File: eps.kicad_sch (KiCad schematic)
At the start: 14 parts

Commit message: added
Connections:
- net GND: now reaches SC1.2 (-), SC2.2 (-), SC3.2 (-), SC4.2 (-), SC5.2 (-), SC6.2 (-)
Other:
- sheet BatteryCharger ports: added gnd; removed none
- sheet BatteryCharger1 ports: added gnd; removed none
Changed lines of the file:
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@@
   (junction (at 64.77 64.77) (diameter 0) (color 0 0 0 0)
   )
+  (junction (at 46.99 121.92) (diameter 0) (color 0 0 0 0)
+  )
   (junction (at 46.99 80.01) (diameter 0) (color 0 0 0 0)
   )
@@
     (stroke (width 0) (type default))
   )
+  (wire (pts (xy 100.33 67.31) (xy 95.25 67.31))
+    (stroke (width 0) (type default))
+  )
   (wire (pts (xy 125.73 107.95) (xy 130.81 107.95))
     (stroke (width 0) (type default))
@@
     (stroke (width 0) (type default))
   )
+  (wire (pts (xy 97.79 110.49) (xy 102.87 110.49))
+    (stroke (width 0) (type default))
+  )
   (wire (pts (xy 138.43 85.09) (xy 138.43 107.95))
     (stroke (width 0) (type default))
@@
     (stroke (width 0) (type default))
   )
+  (wire (pts (xy 95.25 67.31) (xy 95.25 72.39))
+    (stroke (width 0) (type default))
+  )
   (wire (pts (xy 46.99 80.01) (xy 46.99 93.98))
     (stroke (width 0) (type default))
@@
     (stroke (width 0) (type default))
   )
+  (wire (pts (xy 97.79 118.11) (xy 97.79 110.49))
+    (stroke (width 0) (type default))
+  )
   (symbol (lib_id "Device:Solar_Cells") (at 52.07 93.98 270) (unit 1)
     (in_bom yes) (on_board yes) (dnp no) (fields_autoplaced)
@@
     )
   )
+  (symbol (lib_id "power:GND") (at 46.99 121.92 0) (unit 1)
+    (in_bom yes) (on_board yes) (dnp no) (fields_autoplaced)
+    (property "Reference" "#PWR04" (at 46.99 128.27 0)
+      (effects (font (size 1.27 1.27)) hide)
+    )
+    (property "Value" "GND" (at 46.99 127 0)
+      (effects (font (size 1.27 1.27)))
+    )
+    (property "Footprint" "" (at 46.99 121.92 0)
+      (effects (font (size 1.27 1.27)) hide)
+    )
+    (property "Datasheet" "" (at 46.99 121.92 0)
+      (effects (font (size 1.27 1.27)) hide)
+    )
+    (pin "1")
+    (instances
+      (project "eps"
+        (path "/d1becec8-2a81-45a7-bfc6-f9ad93456edc"
+          (reference "#PWR04") (unit 1)
+        )
+      )
+    )
+  )
   (symbol (lib_id "Device:D_Schottky") (at 60.96 121.92 180) (unit 1)
     (in_bom yes) (on_board yes) (dnp no) (fields_autoplaced)
@@
     )
   )
+  (symbol (lib_id "power:GND") (at 97.79 118.11 0) (unit 1)
+    (in_bom yes) (on_board yes) (dnp no) (fields_autoplaced)
+    (property "Reference" "#PWR03" (at 97.79 124.46 0)
+      (effects (font (size 1.27 1.27)) hide)
+    )
+    (property "Value" "GND" (at 97.79 123.19 0)
+      (effects (font (size 1.27 1.27)))
+    )
+    (property "Footprint" "" (at 97.79 118.11 0)
+      (effects (font (size 1.27 1.27)) hide)
+    )
+    (property "Datasheet" "" (at 97.79 118.11 0)
+      (effects (font (size 1.27 1.27)) hide)
+    )
+    (pin "1")
+    (instances
+      (project "eps"
+        (path "/d1becec8-2a81-45a7-bfc6-f9ad93456edc"
+          (reference "#PWR03") (unit 1)
+        )
+      )
+    )
+  )
   (symbol (lib_id "Device:Solar_Cells") (at 52.07 64.77 270) (unit 1)
     (in_bom yes) (on_board yes) (dnp no) (fields_autoplaced)
@@
         (path "/d1becec8-2a81-45a7-bfc6-f9ad93456edc"
           (reference "SC1") (unit 1)
+        )
+      )
+    )
+  )
+  (symbol (lib_id "power:GND") (at 95.25 72.39 0) (unit 1)
+    (in_bom yes) (on_board yes) (dnp no) (fields_autoplaced)
+    (property "Reference" "#PWR02" (at 95.25 78.74 0)
+      (effects (font (size 1.27 1.27)) hide)
+    )
+    (property "Value" "GND" (at 95.25 77.47 0)
+      (effects (font (size 1.27 1.27)))
+    )
+    (property "Footprint" "" (at 95.25 72.39 0)
+      (effects (font (size 1.27 1.27)) hide)
+    )
+    (property "Datasheet" "" (at 95.25 72.39 0)
+      (effects (font (size 1.27 1.27)) hide)
+    )
+    (pin "1")
+    (instances
+      (project "eps"
+        (path "/d1becec8-2a81-45a7-bfc6-f9ad93456edc"
+          (reference "#PWR02") (unit 1)
         )
       )
@@
       (effects (font (size 1.27 1.27)) (justify right))
     )
+    (pin "gnd" input (at 102.87 110.49 180)
+      (effects (font (size 1.27 1.27)) (justify left))
+    )
     (instances
       (project "eps"
@@
       (effects (font (size 1.27 1.27)) (justify right))
     )
-    (instances
+    (pin "gnd" input (at 100.33 67.31 180)
+      (effects (font (size 1.27 1.27)) (justify left))
+    )
+    (instances

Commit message: v0.1Hydrogen
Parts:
- removed D7, D8: D_Schottky, symbol Device:D_Schottky
- D1, D2, D3, D4, D5, D6: footprint (none) -> Diode_THT:D_DO-35_SOD27_P7.62mm_Horizontal
- SC1, SC2, SC3, SC4, SC5, SC6: footprint (none) -> Connector_PinHeader_1.00mm:PinHeader_2x01_P1.00mm_Vertical
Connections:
- net BatteryCharger1/in is gone; now on net BatteryCharger/in: D4.1 (K), D5.1 (K), D6.1 (K)
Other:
- removed sheet BatteryCharger1
- sheet BatteryCharger ports: added none; removed gnd

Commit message: Solved errors
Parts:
- added J2: Conn_01x02_Pin, Connector_PinHeader_2.00mm:PinHeader_1x02_P2.00mm_Vertical, symbol Connector:Conn_01x02_Pin
- SC1, SC2, SC3, SC4, SC5, SC6: footprint Connector_PinHeader_1.00mm:PinHeader_2x01_P1.00mm_Vertical -> Connector_PinHeader_2.00mm:PinHeader_1x02_P2.00mm_Vertical
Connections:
- net GND: now also J2.1 (Pin_1)
- new net BatteryCharger/load: J2.2 (Pin_2)

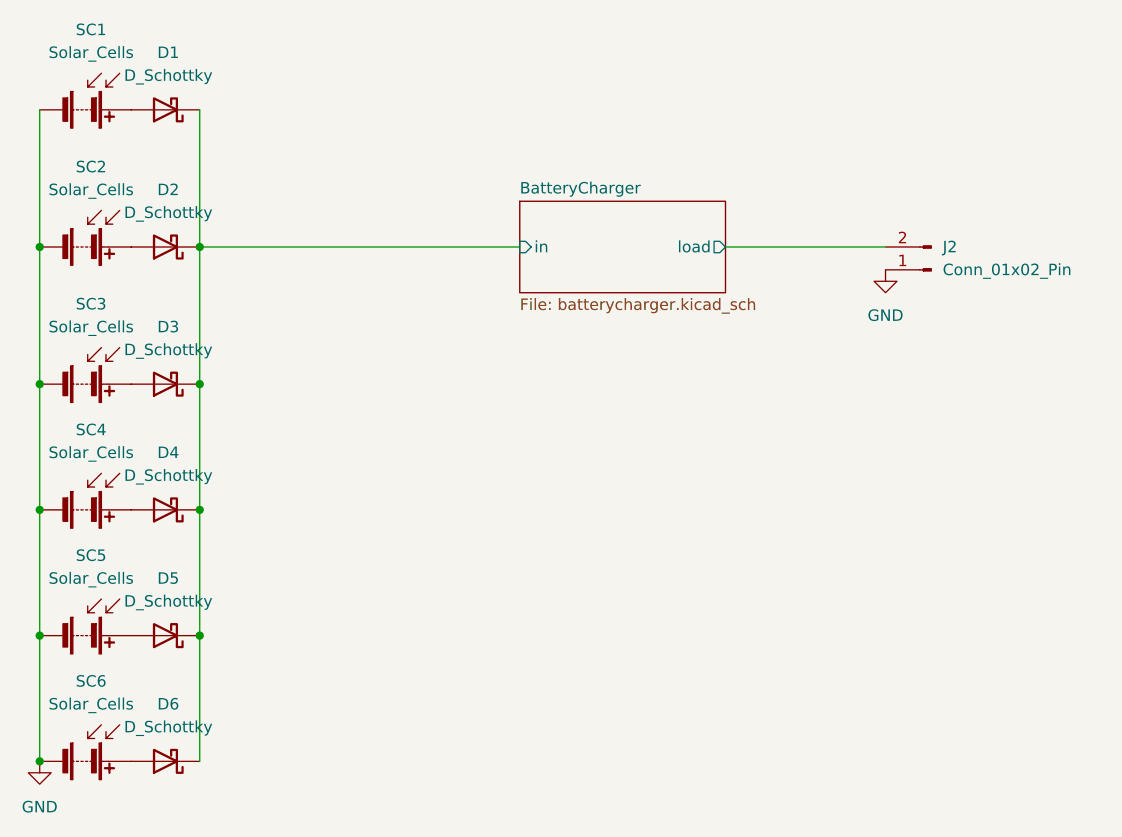
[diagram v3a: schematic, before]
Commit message: Adding sensors
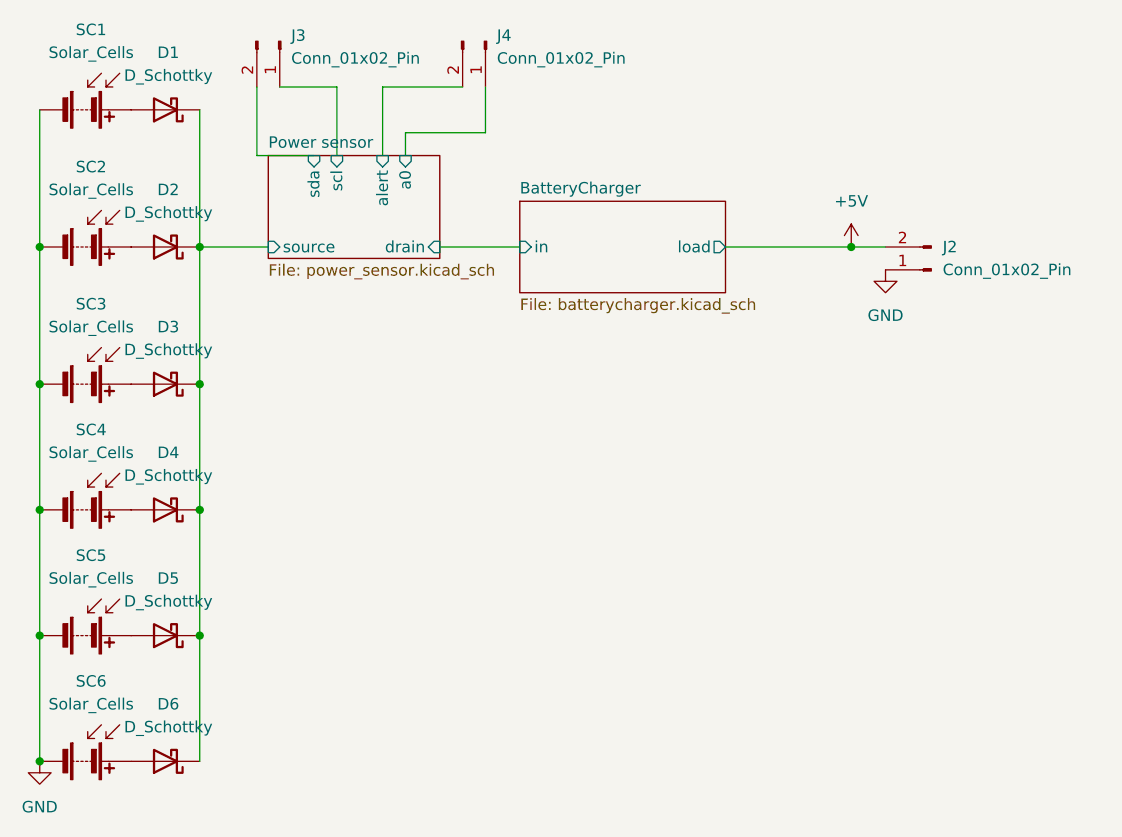
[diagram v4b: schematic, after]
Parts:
- added J3, J4: Conn_01x02_Pin, Connector_PinHeader_2.00mm:PinHeader_1x02_P2.00mm_Vertical, symbol Connector:Conn_01x02_Pin
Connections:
- net BatteryCharger/in: no longer D1.1 (K), D2.1 (K), D3.1 (K), D4.1 (K), D5.1 (K), D6.1 (K)
- net BatteryCharger/load renamed +5V
- new net Power sensor/a0: J4.1 (Pin_1)
- new net Power sensor/alert: J4.2 (Pin_2)
- new net Power sensor/scl: J3.1 (Pin_1)
- new net Power sensor/sda: J3.2 (Pin_2)
- new net Power sensor/source: D1.1 (K), D2.1 (K), D3.1 (K), D4.1 (K), D5.1 (K), D6.1 (K)
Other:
- added sheet Power sensor (power_sensor.kicad_sch)

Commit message: Added
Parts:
- added J5, J6: Conn_01x02_Pin, Connector_PinHeader_2.00mm:PinHeader_1x02_P2.00mm_Vertical, symbol Connector:Conn_01x02_Pin
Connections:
- new net BatteryCharger/a0: J5.2 (Pin_2)
- new net BatteryCharger/alert: J6.1 (Pin_1)
- new net BatteryCharger/scl: J6.2 (Pin_2)
- new net BatteryCharger/sda: J5.1 (Pin_1)
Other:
- sheet BatteryCharger ports: added a0, alert, scl, sda; removed none

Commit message: new design
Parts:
- removed J3, J4, J5, J6: Conn_01x02_Pin, Connector_PinHeader_2.00mm:PinHeader_1x02_P2.00mm_Vertical, symbol Connector:Conn_01x02_Pin
- J2, SC1, SC2, SC3, SC4, SC5, SC6: footprint Connector_PinHeader_2.00mm:PinHeader_1x02_P2.00mm_Vertical -> Connector_PinHeader_2.54mm:PinHeader_1x02_P2.54mm_Vertical
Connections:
- net Power sensor/source is gone; now on net BatteryCharger/in: D1.1 (K), D2.1 (K), D3.1 (K), D4.1 (K), D5.1 (K), D6.1 (K)
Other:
- removed sheet Power sensor
- sheet BatteryCharger ports: added none; removed a0, alert, scl, sda
